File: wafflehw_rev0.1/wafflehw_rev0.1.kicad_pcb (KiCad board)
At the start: 2 copper layers, 42 x 66 mm, 37 parts, among them J1 USB_C_Receptacle_USB2.0_14P, J2 OLED_Disp, J3 FH34SRJ-30S-0.5SH, J4 BATT, J5 LCD_BL, Q1 2N7002K, Q2 2N7002H, Q3 2N7002H, SW1 SW_Push, SW2 BTN_UP, SW3 BTN_DN, SW4 BTN_OK, U1 Ai-Thinker-Ra-01, U2 MCP73831-2-OT, U3 ESP32-S3-WROOM-1, U4 MIC5219-3.3YM5

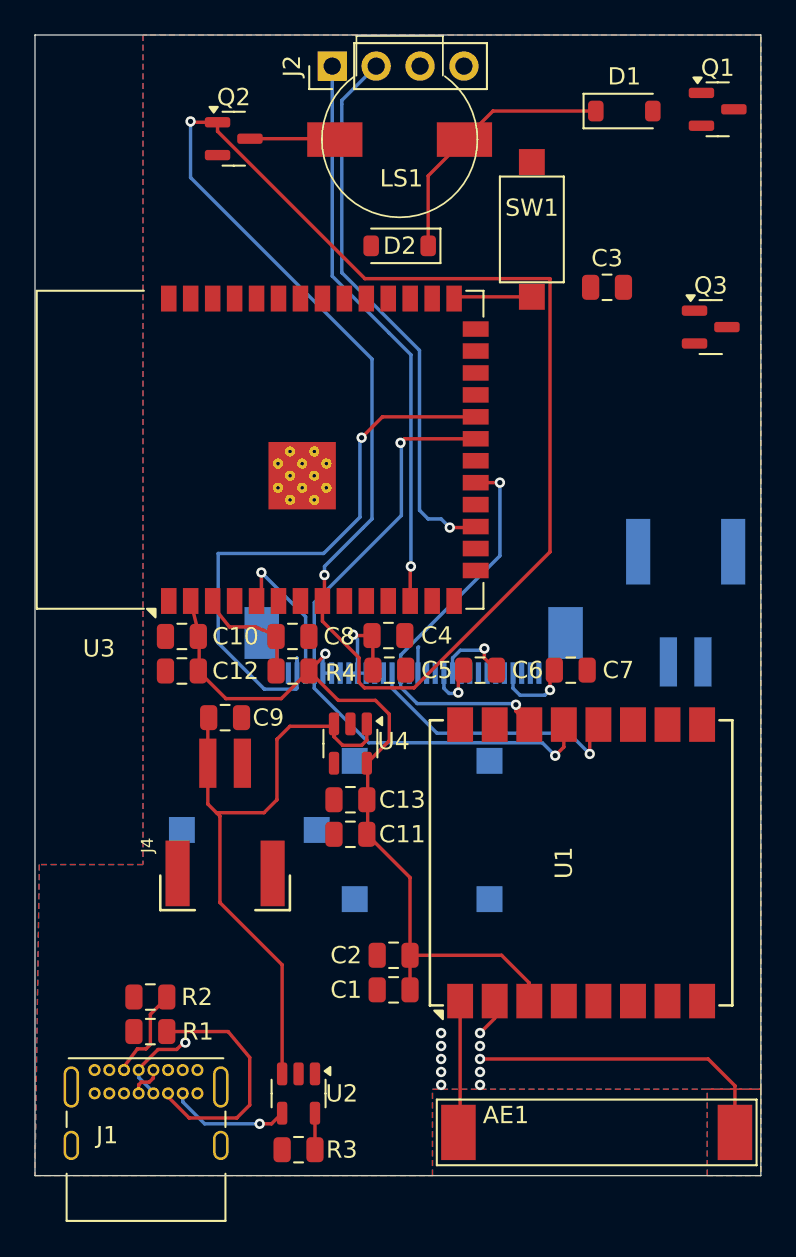
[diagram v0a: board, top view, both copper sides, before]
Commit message: Schematic improvements
- Changed to two LDOs and add ferrite beads
- Changed battery charging IC to pin compatible TP4054
- USB connector changed to more common variant
- Antenna pad disconnected from ground
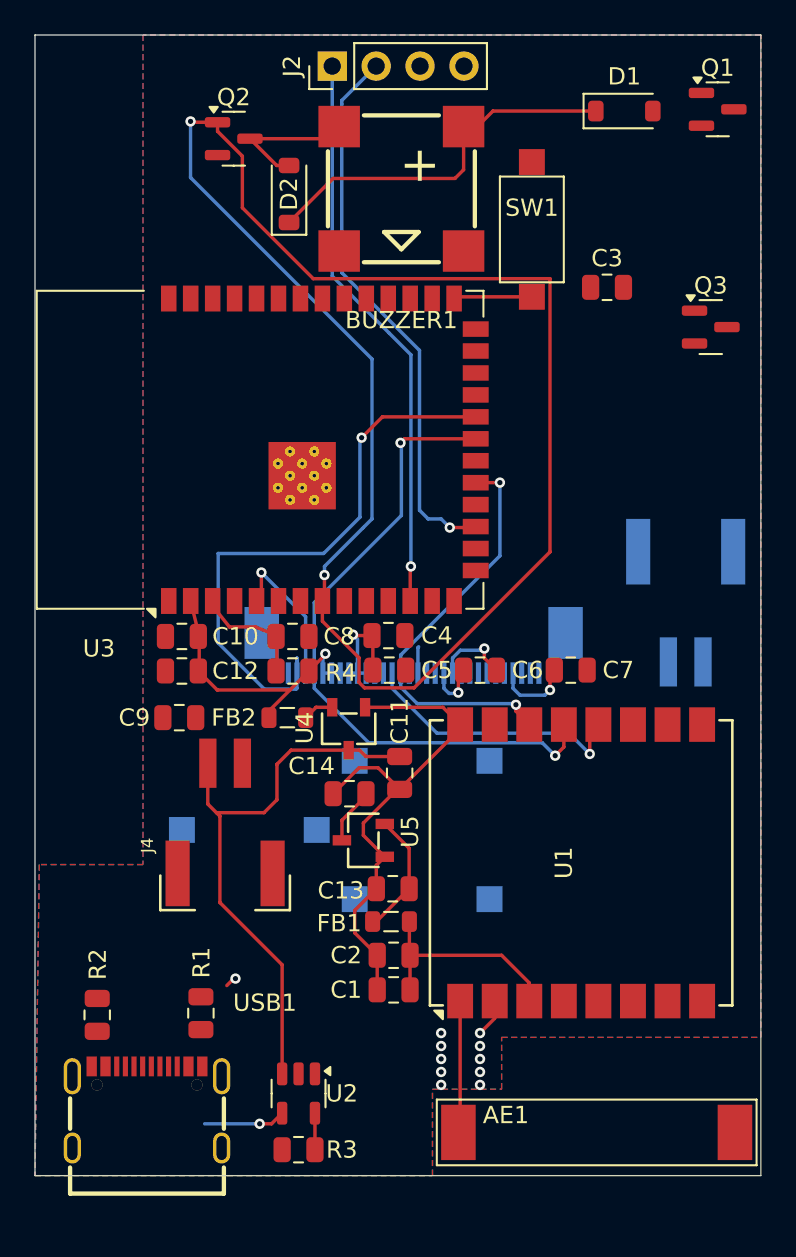
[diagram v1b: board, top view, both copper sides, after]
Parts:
- removed J1: USB_C_Receptacle_USB2.0_14P, Connector_USB:USB_C_Receptacle_GCT_USB4085
- removed LS1: ST-0311T, Waffle2Rev0.1:ST-0311T
- added BUZZER1: MLT-8530, easyeda:BUZ-SMD_4P-L8.5-W8.5-P8.50-BR, F.Cu at (121.2, 38.9)
- added C14: 1u, Capacitor_SMD:C_0805_2012Metric, F.Cu at (118.2, 73.9)
- added FB1: GZ2012D601TF, Inductor_SMD:L_0805_2012Metric, F.Cu at (120.6, 81.3)
- added FB2: GZ2012D601TF, Inductor_SMD:L_0805_2012Metric, F.Cu at (114.6, 69.5)
- added U5: MD57E33QA3, easyeda:SOT-23-3_L2.9-W1.6-P1.90-LS2.8-BR, F.Cu at (119.0, 76.6)
- added USB1: TYPE-C16PIN, easyeda:USB-C-SMD_TYPE-C16PIN, F.Cu at (106.5, 92.0)
- C11, C9: value 10u -> 1u
- C13: value 100n -> 1u
- Q1: value 2N7002K -> AO3400A
- Q2, Q3: value 2N7002H -> AO3400A
- U2: value MCP73831-2-OT -> TP4054
- U4: value MIC5219-3.3YM5 -> MD57E33QA3; footprint Package_TO_SOT_SMD:SOT-23-5 -> easyeda:SOT-23-3_L2.9-W1.6-P1.90-LS2.8-BR
- moved D2 7.07 mm to (114.7, 39.2), turned to 90 degrees
- moved C13 5.70 mm to (120.7, 79.4)
- moved C11 4.55 mm to (121.1, 72.7), turned to -90 degrees
- moved R2 3.24 mm to (103.6, 86.7), turned to 90 degrees
- moved R1 3.11 mm to (109.6, 86.6), turned to 90 degrees
- moved C9 2.65 mm to (108.3, 69.5), turned to 180 degrees
- moved U4 0.87 mm to (118.2, 70.1), turned to 90 degrees
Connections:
- AE1 pad 2: GND -> unconnected-(AE1-Shield-Pad2)
- C1 pad 1: +3.3V -> +3.3V_RF
- C11 pad 1: +3.3V -> +BATT
- C13 pad 1: +3.3V -> Net-(U5-VOUT)
- C2 pad 1: +3.3V -> +3.3V_RF
- C9 pad 1: +BATT -> Net-(U4-VOUT)
- U1 pad 3: +3.3V -> +3.3V_RF
- U4 pad 1: +BATT -> GND
- U4 pad 2: GND -> Net-(U4-VOUT)
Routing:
- net +3.3V: track 47.0 -> 21.0 mm
- net +BATT: track 35.9 -> 51.8 mm
- net +3.3V_RF: track 0.00 -> 12.7 mm
- net GND: track 21.8 -> 34.2 mm
- net Net-(U5-VOUT): track 0.00 -> 7.23 mm
- net ESP32_D+: track 5.24 -> 0.57 mm
- net Net-(D2-A): track 0.00 -> 2.90 mm
- net +5V: track 7.02 -> 4.74 mm
- net ESP32_D-: track 1.97 -> 0.00 mm
- net Net-(U4-VOUT): track 0.00 -> 1.79 mm
- net BUZZER: track 94.0 -> 95.8 mm
